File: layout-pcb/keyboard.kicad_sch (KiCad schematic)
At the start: 285 parts, among them J1 USB_C_Receptacle_USB2.0_16P, SW1 SW_Push, U1 RP2040_Stamp

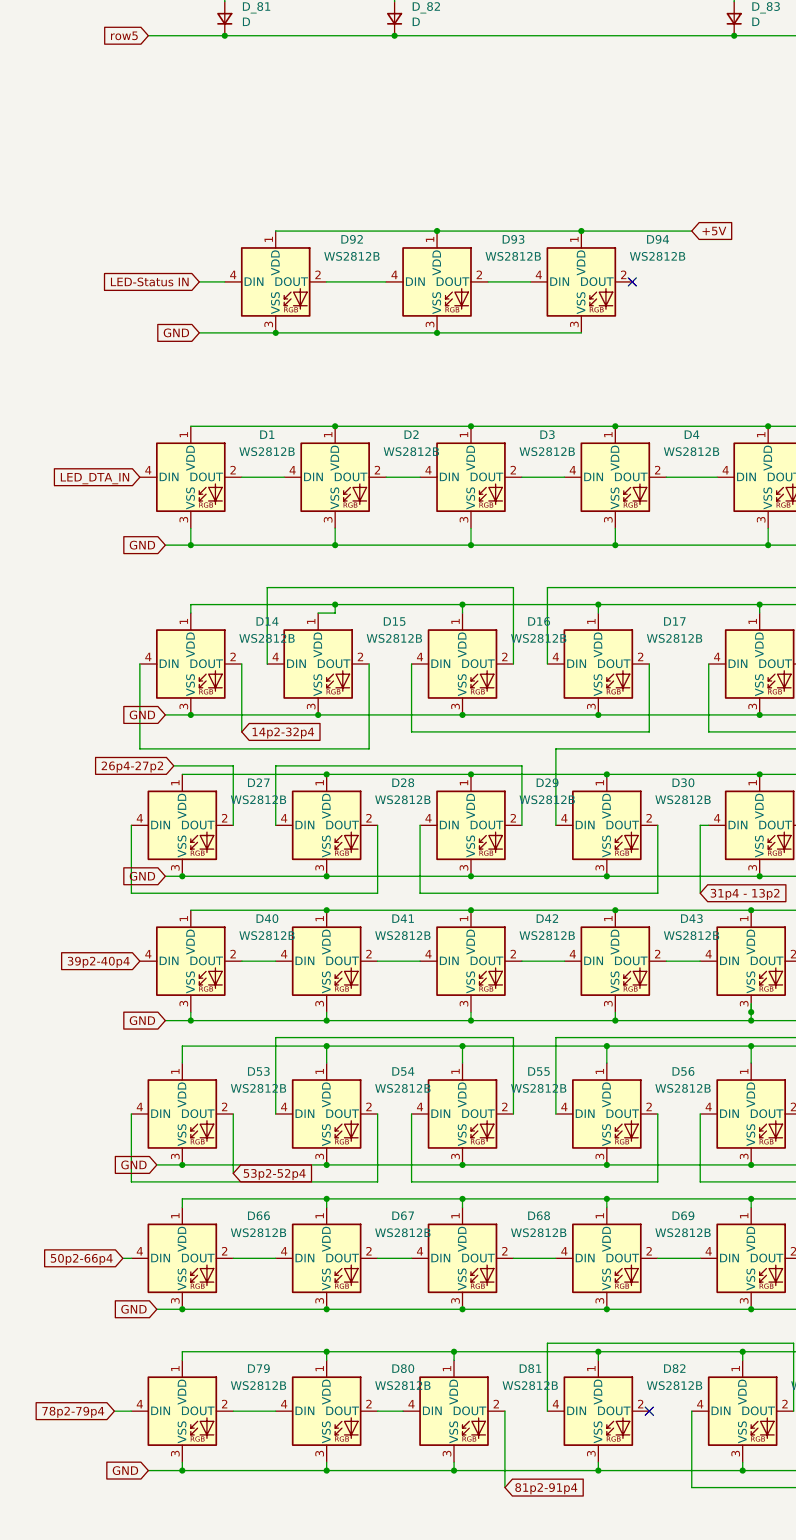
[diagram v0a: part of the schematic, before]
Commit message: pjw WIP - +5V plane done (wrong - incorrect vias)
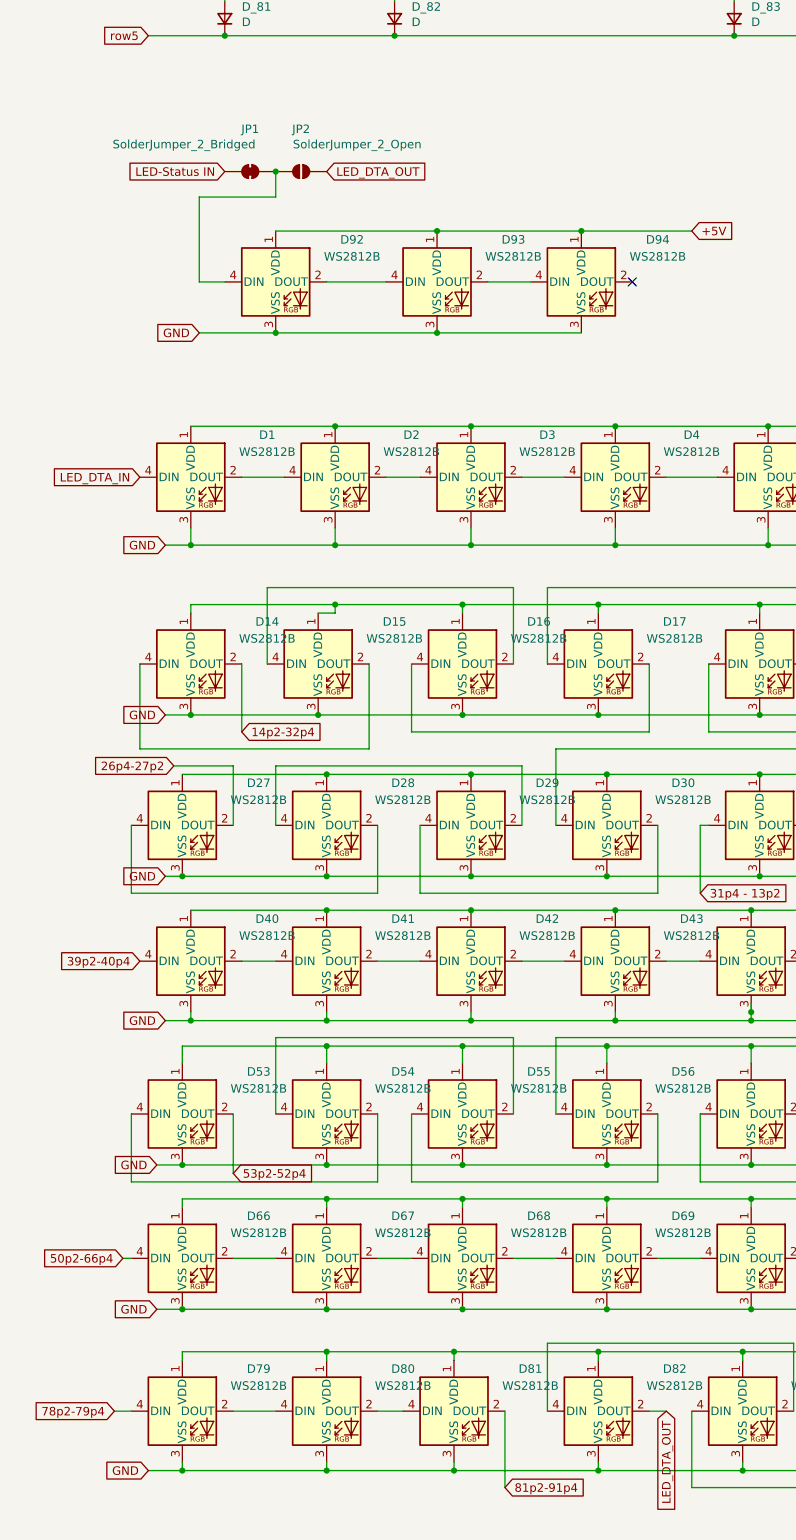
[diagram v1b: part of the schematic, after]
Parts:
- added JP1: SolderJumper_2_Bridged, Jumper:SolderJumper-2_P1.3mm_Bridged_Pad1.0x1.5mm, symbol Jumper:SolderJumper_2_Bridged
- added JP2: SolderJumper_2_Open, symbol Jumper:SolderJumper_2_Open
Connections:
- net LED-Status IN: now also JP1.1 (A); no longer D92.4 (DIN)
- net LED_DTA_OUT: now reaches D82.2 (DOUT)
- net LED_DTA_OUT: now also JP2.2 (B)
- new net: D92.4 (DIN), JP1.2 (B), JP2.1 (A)
- no-connect marks 16 -> 15
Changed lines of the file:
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@@
 	)
 	(junction
+		(at 41.91 208.28)
+		(diameter 0)
+		(color 0 0 0 0)
+	)
+	(junction
 		(at 91.44 378.46)
 		(diameter 0)
@@
 	)
 	(no_connect
-		(at 97.79 393.7)
-	)
-	(no_connect
 		(at 491.49 278.13)
 	)
@@
 	(wire
 		(pts
+			(xy 30.48 212.09) (xy 41.91 212.09)
+		)
+		(stroke
+			(width 0)
+			(type default)
+		)
+	)
+	(wire
+		(pts
 			(xy 29.21 318.77) (xy 49.53 318.77)
 		)
@@
 	(wire
 		(pts
+			(xy 97.79 393.7) (xy 100.33 393.7)
+		)
+		(stroke
+			(width 0)
+			(type default)
+		)
+	)
+	(wire
+		(pts
 			(xy 223.52 100.33) (xy 223.52 74.93)
 		)
@@
 	(wire
 		(pts
+			(xy 41.91 212.09) (xy 41.91 208.28)
+		)
+		(stroke
+			(width 0)
+			(type default)
+		)
+	)
+	(wire
+		(pts
 			(xy 168.91 326.39) (xy 172.72 326.39)
 		)
@@
 	(wire
 		(pts
+			(xy 30.48 224.79) (xy 30.48 212.09)
+		)
+		(stroke
+			(width 0)
+			(type default)
+		)
+	)
+	(wire
+		(pts
 			(xy 237.49 130.81) (xy 237.49 132.08)
 		)
@@
 		)
 	)
+	(global_label "LED_DTA_OUT"
+		(shape input)
+		(at 100.33 393.7 270)
+		(fields_autoplaced yes)
+		(effects
+			(font
+				(size 1.27 1.27)
+			)
+			(justify right)
+		)
+		(property "Intersheetrefs" "${INTERSHEET_REFS}"
+			(at 100.33 408.3681 90)
+			(effects
+				(font
+					(size 1.27 1.27)
+				)
+				(justify right)
+				(hide yes)
+			)
+		)
+	)
 	(global_label "LED_GND"
 		(shape input)
@@
 		)
 	)
+	(global_label "LED_DTA_OUT"
+		(shape input)
+		(at 49.53 208.28 0)
+		(fields_autoplaced yes)
+		(effects
+			(font
+				(size 1.27 1.27)
+			)
+			(justify left)
+		)
+		(property "Intersheetrefs" "${INTERSHEET_REFS}"
+			(at 64.1981 208.28 0)
+			(effects
+				(font
+					(size 1.27 1.27)
+				)
+				(justify left)
+				(hide yes)
+			)
+		)
+	)
 	(global_label "col0"
 		(shape input)
@@
 	(global_label "LED-Status IN"
 		(shape input)
-		(at 30.48 224.79 180)
+		(at 34.29 208.28 180)
 		(fields_autoplaced yes)
 		(effects
@@
 		)
 		(property "Intersheetrefs" "${INTERSHEET_REFS}"
-			(at 14.2396 224.79 0)
+			(at 18.0496 208.28 0)
 			(effects
 				(font
@@
 	)
 	(symbol
+		(lib_id "Jumper:SolderJumper_2_Bridged")
+		(at 38.1 208.28 0)
+		(unit 1)
+		(exclude_from_sim yes)
+		(in_bom no)
+		(on_board yes)
+		(dnp no)
+		(property "Reference" "JP1"
+			(at 38.1 201.93 0)
+			(effects
+				(font
+					(size 1.27 1.27)
+				)
+			)
+		)
+		(property "Value" "SolderJumper_2_Bridged"
+			(at 28.194 204.216 0)
+			(effects
+				(font
+					(size 1.27 1.27)
+				)
+			)
+		)
+		(property "Footprint" "Jumper:SolderJumper-2_P1.3mm_Bridged_Pad1.0x1.5mm"
+			(at 38.1 208.28 0)
+			(effects
+				(font
+					(size 1.27 1.27)
+				)
+				(hide yes)
+			)
+		)
+		(property "Datasheet" "~"
+			(at 38.1 208.28 0)
+			(effects
+				(font
+					(size 1.27 1.27)
+				)
+				(hide yes)
+			)
+		)
+		(property "Description" "Solder Jumper, 2-pole, closed/bridged"
+			(at 38.1 208.28 0)
+			(effects
+				(font
+					(size 1.27 1.27)
+				)
+				(hide yes)
+			)
+		)
+		(pin "2"
+		)
+		(pin "1"
+		)
+		(instances
+			(project ""
+				(path "/e0cf6e22-5f1c-474f-bc7a-bb6048e02412"
+					(reference "JP1")
+					(unit 1)
+				)
+			)
+		)
+	)
+	(symbol
 		(lib_id "MX_Alps_Hybrid:MX-NoLED")
 		(at 264.16 25.4 0)
@@
 					(unit 1)
 				)
+			)
+		)
+	)
+	(symbol
+		(lib_id "Jumper:SolderJumper_2_Open")
+		(at 45.72 208.28 0)
+		(unit 1)
+		(exclude_from_sim yes)
+		(in_bom no)
+		(on_board yes)
+		(dnp no)
+		(property "Reference" "JP2"
+			(at 45.72 201.93 0)
+			(effects
+				(font
+					(size 1.27 1.27)
+				)
+			)
+		)
+		(property "Value" "SolderJumper_2_Open"
+			(at 54.102 204.216 0)
+			(effects
+				(font
+					(size 1.27 1.27)
+				)
+			)
+		)
+		(property "Footprint" ""
+			(at 45.72 208.28 0)
+			(effects
+				(font
+					(size 1.27 1.27)
+				)
+				(hide yes)
+			)
+		)
+		(property "Datasheet" "~"
+			(at 45.72 208.28 0)
+			(effects
+				(font
+					(size 1.27 1.27)
+				)
+				(hide yes)
+			)
+		)
+		(property "Description" "Solder Jumper, 2-pole, open"
+			(at 45.72 208.28 0)
+			(effects
+				(font
+					(size 1.27 1.27)
+				)
+				(hide yes)
+			)
+		)
+		(pin "2"
+		)
+		(pin "1"
+		)
+		(instances
+			(project ""
+				(path "/e0cf6e22-5f1c-474f-bc7a-bb6048e02412"
+					(reference "JP2")
+					(unit 1)
+				)

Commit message: PCB Changes WIP
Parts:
- removed JP2: SolderJumper_2_Open, symbol Jumper:SolderJumper_2_Open
- added JP3: SolderJumper_2_Open, Jumper:SolderJumper-2_P1.3mm_Open_Pad1.0x1.5mm, symbol Jumper:SolderJumper_2_Open
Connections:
- net LED_DTA_OUT: now also JP3.2 (B)
- net at D92.4 (DIN), JP1.2 (B): now also JP3.1 (A)
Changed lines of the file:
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@@
 	)
 	(junction
+		(at 41.91 208.28)
+		(diameter 0)
+		(color 0 0 0 0)
+	)
+	(junction
 		(at 401.32 100.33)
 		(diameter 0)
@@
 	)
 	(junction
-		(at 41.91 208.28)
-		(diameter 0)
-		(color 0 0 0 0)
-	)
-	(junction
 		(at 91.44 378.46)
 		(diameter 0)
@@
 	)
 	(symbol
+		(lib_id "Jumper:SolderJumper_2_Open")
+		(at 45.72 208.28 0)
+		(unit 1)
+		(exclude_from_sim yes)
+		(in_bom no)
+		(on_board yes)
+		(dnp no)
+		(property "Reference" "JP3"
+			(at 45.72 201.93 0)
+			(effects
+				(font
+					(size 1.27 1.27)
+				)
+			)
+		)
+		(property "Value" "SolderJumper_2_Open"
+			(at 54.102 204.47 0)
+			(effects
+				(font
+					(size 1.27 1.27)
+				)
+			)
+		)
+		(property "Footprint" "Jumper:SolderJumper-2_P1.3mm_Open_Pad1.0x1.5mm"
+			(at 45.72 208.28 0)
+			(effects
+				(font
+					(size 1.27 1.27)
+				)
+				(hide yes)
+			)
+		)
+		(property "Datasheet" "~"
+			(at 45.72 208.28 0)
+			(effects
+				(font
+					(size 1.27 1.27)
+				)
+				(hide yes)
+			)
+		)
+		(property "Description" "Solder Jumper, 2-pole, open"
+			(at 45.72 208.28 0)
+			(effects
+				(font
+					(size 1.27 1.27)
+				)
+				(hide yes)
+			)
+		)
+		(pin "2"
+		)
+		(pin "1"
+		)
+		(instances
+			(project ""
+				(path "/e0cf6e22-5f1c-474f-bc7a-bb6048e02412"
+					(reference "JP3")
+					(unit 1)
+				)
+			)
+		)
+	)
+	(symbol
 		(lib_id "Device:D_Small")
 		(at 186.69 134.62 90)
@@
 					(unit 1)
 				)
-			)
-		)
-	)
-	(symbol
-		(lib_id "Jumper:SolderJumper_2_Open")
-		(at 45.72 208.28 0)
-		(unit 1)
-		(exclude_from_sim yes)
-		(in_bom no)
-		(on_board yes)
-		(dnp no)
-		(property "Reference" "JP2"
-			(at 45.72 201.93 0)
-			(effects
-				(font
-					(size 1.27 1.27)
-				)
-			)
-		)
-		(property "Value" "SolderJumper_2_Open"
-			(at 54.102 204.216 0)
-			(effects
-				(font
-					(size 1.27 1.27)
-				)
-			)
-		)
-		(property "Footprint" ""
-			(at 45.72 208.28 0)
-			(effects
-				(font
-					(size 1.27 1.27)
-				)
-				(hide yes)
-			)
-		)
-		(property "Datasheet" "~"
-			(at 45.72 208.28 0)
-			(effects
-				(font
-					(size 1.27 1.27)
-				)
-				(hide yes)
-			)
-		)
-		(property "Description" "Solder Jumper, 2-pole, open"
-			(at 45.72 208.28 0)
-			(effects
-				(font
-					(size 1.27 1.27)
-				)
-				(hide yes)
-			)
-		)
-		(pin "2"
-		)
-		(pin "1"
-		)
-		(instances
-			(project ""
-				(path "/e0cf6e22-5f1c-474f-bc7a-bb6048e02412"
-					(reference "JP2")
-					(unit 1)
-				)
